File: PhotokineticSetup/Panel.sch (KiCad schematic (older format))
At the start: 11 parts, among them J10 Male SMA, J11 Male SMA, J12 Male SMA, J13 Male SMA, J9 DB9_Female, SW1 SW_SPDT, SW2 SW_SPDT

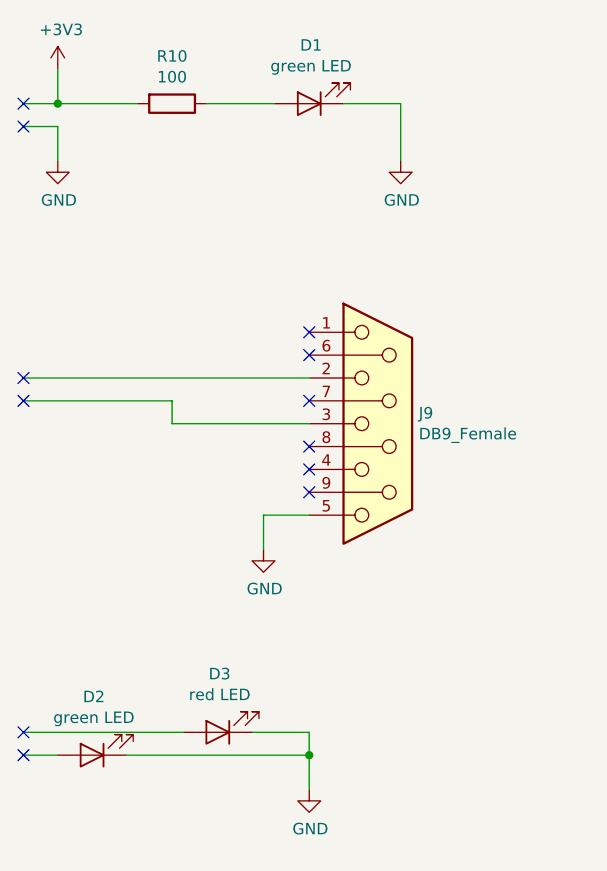
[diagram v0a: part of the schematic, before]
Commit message: Clearer optocouplers outputs and stronger input
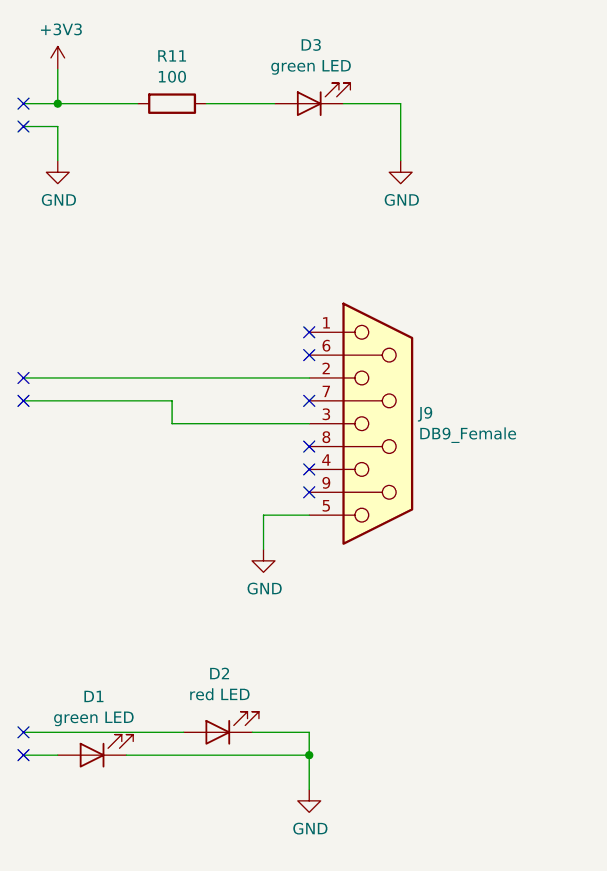
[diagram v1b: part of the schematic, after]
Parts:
- renumbered D2 to D1, D3 to D2, D1 to D3, R10 to R11
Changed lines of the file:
@@
 $EndDescr
 $Comp
-L power:+3V3 #PWR0116
+L power:+3V3 #PWR0122
 U 1 1 60CE5FC0
 P 2050 1400
-F 0 "#PWR0116" H 2050 1250 50  0001 C CNN
+F 0 "#PWR0122" H 2050 1250 50  0001 C CNN
 F 1 "+3V3" H 2065 1573 50  0000 C CNN
 F 2 "" H 2050 1400 50  0001 C CNN
@@
 	2050 1650 2050 1800
 $Comp
-L power:GND #PWR0117
+L power:GND #PWR0123
 U 1 1 60CE6008
 P 2050 1800
-F 0 "#PWR0117" H 2050 1550 50  0001 C CNN
+F 0 "#PWR0123" H 2050 1550 50  0001 C CNN
 F 1 "GND" H 2055 1627 50  0000 C CNN
 F 2 "" H 2050 1800 50  0001 C CNN
@@
 	2050 1550 2050 1400
 $Comp
-L Device:LED D1
+L Device:LED D3
 U 1 1 60CE60E0
 P 3150 1550
-F 0 "D1" H 3142 1295 50  0000 C CNN
+F 0 "D3" H 3142 1295 50  0000 C CNN
 F 1 "green LED" H 3142 1386 50  0000 C CNN
 F 2 "" H 3150 1550 50  0001 C CNN
@@
 	3550 1550 3550 1800
 $Comp
-L power:GND #PWR0118
+L power:GND #PWR0124
 U 1 1 60CE6258
 P 3550 1800
-F 0 "#PWR0118" H 3550 1550 50  0001 C CNN
+F 0 "#PWR0124" H 3550 1550 50  0001 C CNN
 F 1 "GND" H 3555 1627 50  0000 C CNN
 F 2 "" H 3550 1800 50  0001 C CNN
@@
 	2950 3350 2950 3500
 $Comp
-L power:GND #PWR0119
+L power:GND #PWR0125
 U 1 1 60CE686E
 P 2950 3500
-F 0 "#PWR0119" H 2950 3250 50  0001 C CNN
+F 0 "#PWR0125" H 2950 3250 50  0001 C CNN
 F 1 "GND" H 2955 3327 50  0000 C CNN
 F 2 "" H 2950 3500 50  0001 C CNN
@@
 $EndComp
 $Comp
-L Device:LED D3
+L Device:LED D2
 U 1 1 60CE707F
 P 2750 4300
-F 0 "D3" H 2742 4045 50  0000 C CNN
+F 0 "D2" H 2742 4045 50  0000 C CNN
 F 1 "red LED" H 2742 4136 50  0000 C CNN
 F 2 "" H 2750 4300 50  0001 C CNN
@@
 	2900 4300 3150 4300
 $Comp
-L power:GND #PWR0120
+L power:GND #PWR0126
 U 1 1 60CE7089
 P 3150 4550
-F 0 "#PWR0120" H 3150 4300 50  0001 C CNN
+F 0 "#PWR0126" H 3150 4300 50  0001 C CNN
 F 1 "GND" H 3155 4377 50  0000 C CNN
 F 2 "" H 3150 4550 50  0001 C CNN
@@
 	1900 4300 2600 4300
 $Comp
-L Device:LED D2
+L Device:LED D1
 U 1 1 60CE73BF
 P 2200 4400
-F 0 "D2" H 2192 4145 50  0000 C CNN
+F 0 "D1" H 2192 4145 50  0000 C CNN
 F 1 "green LED" H 2192 4236 50  0000 C CNN
 F 2 "" H 2200 4400 50  0001 C CNN
@@
 Connection ~ 2050 1550
 $Comp
-L Device:R R10
+L Device:R R11
 U 1 1 60CE7FC7
 P 2550 1550
-F 0 "R10" V 2343 1550 50  0000 C CNN
+F 0 "R11" V 2343 1550 50  0000 C CNN
 F 1 "100" V 2434 1550 50  0000 C CNN
 F 2 "Resistor_THT:R_Axial_DIN0204_L3.6mm_D1.6mm_P7.62mm_Horizontal" V 2480 1550 50  0001 C CNN
@@
 NoConn ~ 2750 6700
 $Comp
-L power:+3V3 #PWR0121
+L power:+3V3 #PWR0127
 U 1 1 60CED7BF
 P 3000 5600
-F 0 "#PWR0121" H 3000 5450 50  0001 C CNN
+F 0 "#PWR0127" H 3000 5450 50  0001 C CNN
 F 1 "+3V3" H 3015 5773 50  0000 C CNN
 F 2 "" H 3000 5600 50  0001 C CNN
@@
 	6700 4050 7000 4050
 $Comp
-L power:GND #PWR0122
+L power:GND #PWR0128
 U 1 1 60CF074C
 P 6700 4200
-F 0 "#PWR0122" H 6700 3950 50  0001 C CNN
+F 0 "#PWR0128" H 6700 3950 50  0001 C CNN
 F 1 "GND" H 6705 4027 50  0000 C CNN
 F 2 "" H 6700 4200 50  0001 C CNN
@@
 	6700 5400 7000 5400
 $Comp
-L power:GND #PWR0123
+L power:GND #PWR0129
 U 1 1 60CF14BE
 P 6700 5550
-F 0 "#PWR0123" H 6700 5300 50  0001 C CNN
+F 0 "#PWR0129" H 6700 5300 50  0001 C CNN
 F 1 "GND" H 6705 5377 50  0000 C CNN
 F 2 "" H 6700 5550 50  0001 C CNN

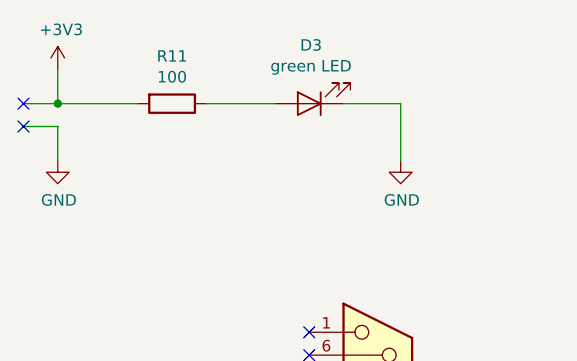
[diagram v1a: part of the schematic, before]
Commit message: LED resistors calculated according to forward voltage
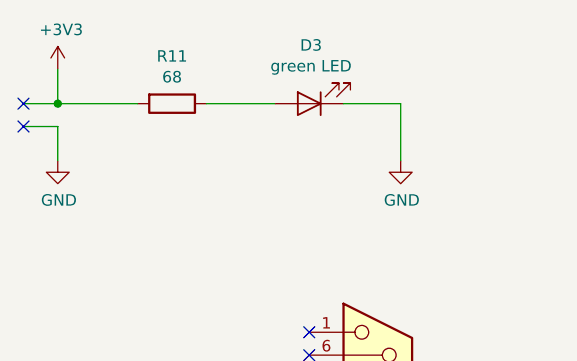
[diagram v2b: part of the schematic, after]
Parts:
- R11: value 100 -> 68
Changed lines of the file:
@@
 P 2550 1550
 F 0 "R11" V 2343 1550 50  0000 C CNN
-F 1 "100" V 2434 1550 50  0000 C CNN
+F 1 "68" V 2434 1550 50  0000 C CNN
 F 2 "Resistor_THT:R_Axial_DIN0204_L3.6mm_D1.6mm_P7.62mm_Horizontal" V 2480 1550 50  0001 C CNN
 F 3 "~" H 2550 1550 50  0001 C CNN
